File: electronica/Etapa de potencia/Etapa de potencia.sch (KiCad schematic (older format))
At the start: 20 parts

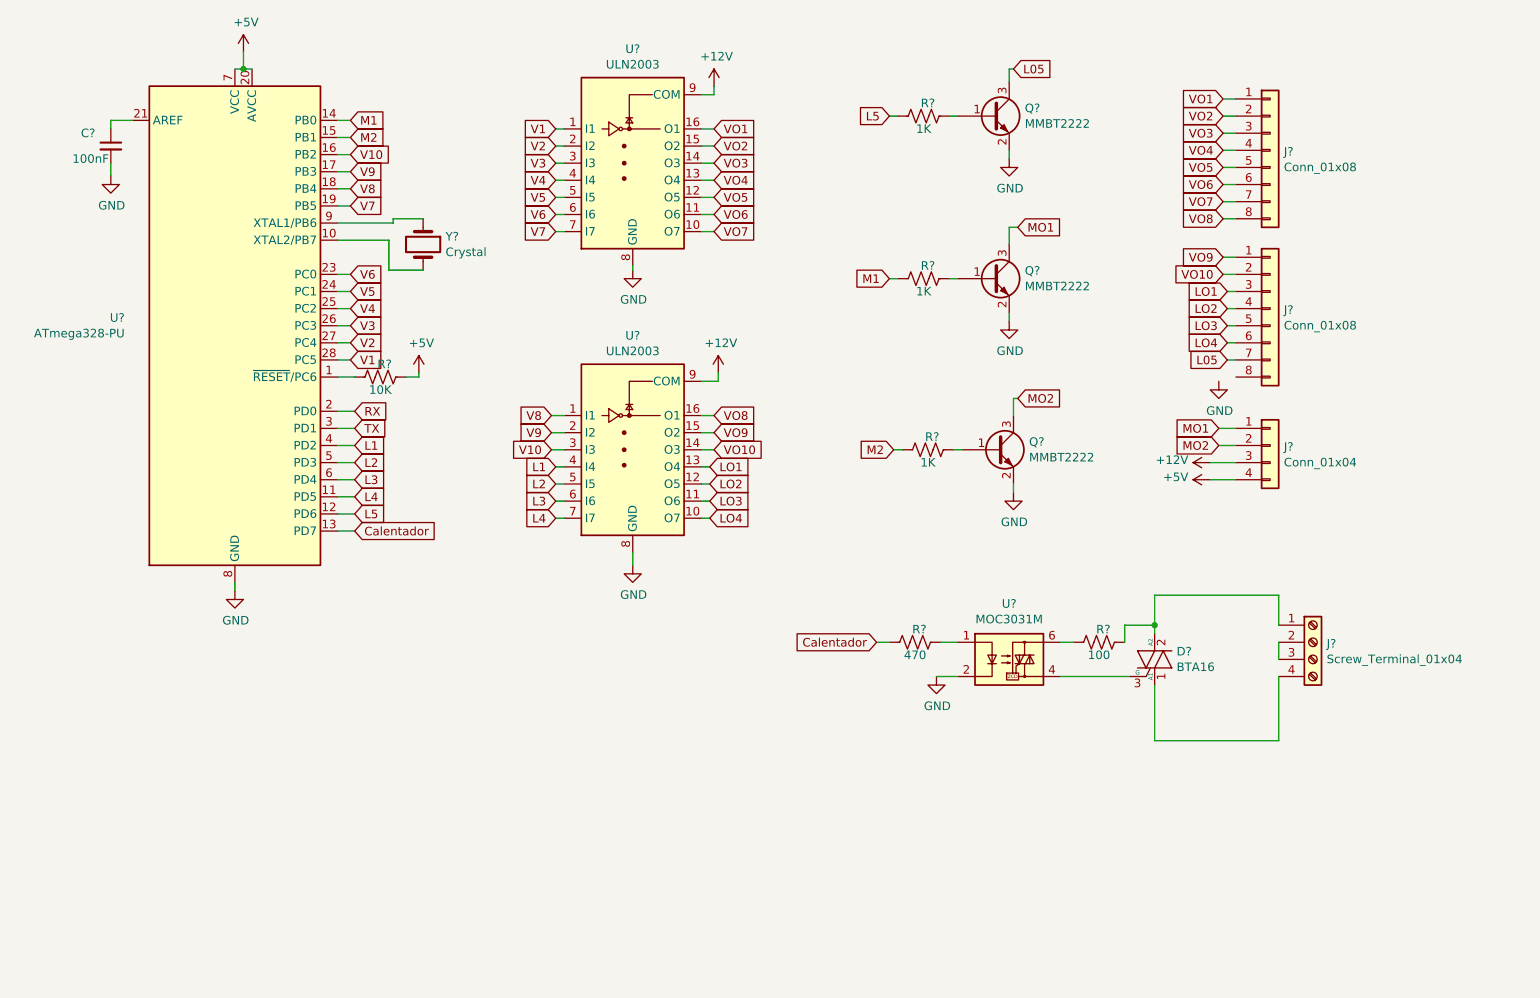
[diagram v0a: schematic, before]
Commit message: Power Stage PCB ready to revision
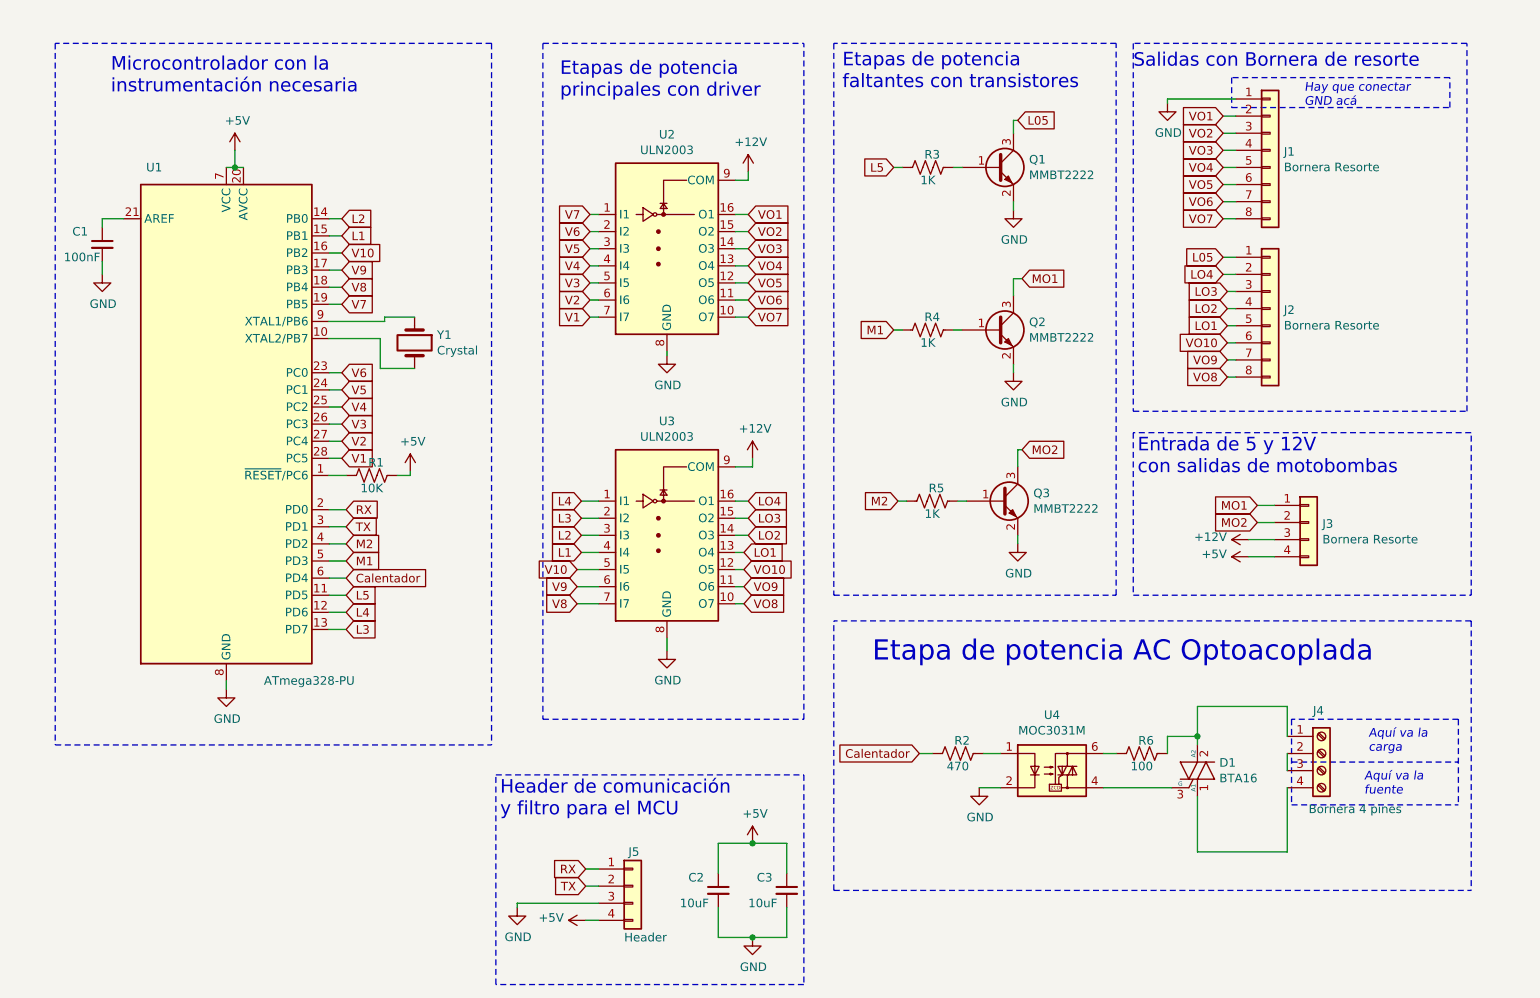
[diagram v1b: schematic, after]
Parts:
- added C2, C3: 10uF, Capacitor_SMD:C_0805_2012Metric_Pad1.15x1.40mm_HandSolder, symbol Device:C_Small
- added J5: Header, Connector_PinHeader_2.54mm:PinHeader_1x04_P2.54mm_Vertical, symbol Connector_Generic:Conn_01x04
- C1: renamed from C?; footprint (none) -> Capacitor_SMD:C_0805_2012Metric_Pad1.15x1.40mm_HandSolder
- D1: renamed from D?; footprint (none) -> Package_TO_SOT_THT:TO-220-3_Horizontal_TabDown
- J1, J2: renamed from J?; value Conn_01x08 -> Bornera Resorte; footprint (none) -> potenciaFootprints:BorneraKF141R_8Pins
- J3: renamed from J?; value Conn_01x04 -> Bornera Resorte; footprint (none) -> potenciaFootprints:BorneraKF141R_4Pins
- J4: renamed from J?; value Screw_Terminal_01x04 -> Bornera 4 pines; footprint (none) -> TerminalBlock:TerminalBlock_Altech_AK300-4_P5.00mm
- R1, R2, R3, R4, R5: renamed from R?; footprint (none) -> Resistor_SMD:R_0805_2012Metric_Pad1.15x1.40mm_HandSolder
- R6: renamed from R?; footprint (none) -> Resistor_THT:R_Axial_DIN0411_L9.9mm_D3.6mm_P12.70mm_Horizontal
- U2, U3: renamed from U?; footprint (none) -> Package_SO:SOIC-16W_5.3x10.2mm_P1.27mm
- U4: renamed from U?; footprint (none) -> Package_DIP:DIP-6_W7.62mm_LongPads
- Y1: renamed from Y?; footprint (none) -> Crystal:Crystal_SMD_0603-2Pin_6.0x3.5mm
- gave numbers to parts that had none: 4
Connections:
- net +5V: now also C2.1, C3.1, J5.4 (Pin_4)
- net Calentador: now also U1.6 (PD4); no longer U1.13 (PD7)
- net GND: now also J1.1 (Pin_1), C2.2, C3.2, J5.3 (Pin_3)
- net L05: now also J2.1 (Pin_1); no longer J2.7 (Pin_7)
- net L1: now also U1.15 (PB1); no longer U1.4 (PD2)
- net L2: now also U1.14 (PB0), U3.3 (I3); no longer U1.5 (PD3), U3.5 (I5)
- net L3: now also U1.13 (PD7), U3.2 (I2); no longer U1.6 (PD4), U3.6 (I6)
- net L4: now also U1.12 (PD6), U3.1 (I1); no longer U1.11 (PD5), U3.7 (I7)
- net L5: now also U1.11 (PD5); no longer U1.12 (PD6)
- net LO1: now also J2.5 (Pin_5); no longer J2.3 (Pin_3)
- net LO2: now also U3.14 (O3); no longer U3.12 (O5)
- net LO3: now also J2.3 (Pin_3), U3.15 (O2); no longer J2.5 (Pin_5), U3.11 (O6)
- net LO4: now also J2.2 (Pin_2), U3.16 (O1); no longer J2.6 (Pin_6), U3.10 (O7)
- net M1: now also U1.5 (PD3); no longer U1.14 (PB0)
- net M2: now also U1.4 (PD2); no longer U1.15 (PB1)
- net RX: now also J5.1 (Pin_1)
- net TX: now also J5.2 (Pin_2)
- net V1: now also U2.7 (I7); no longer U2.1 (I1)
- net V10: now also U3.5 (I5); no longer U3.3 (I3)
- net V2: now also U2.6 (I6); no longer U2.2 (I2)
- net V3: now also U2.5 (I5); no longer U2.3 (I3)
- net V5: now also U2.3 (I3); no longer U2.5 (I5)
- net V6: now also U2.2 (I2); no longer U2.6 (I6)
- net V7: now also U2.1 (I1); no longer U2.7 (I7)
- net V8: now also U3.7 (I7); no longer U3.1 (I1)
- net V9: now also U3.6 (I6); no longer U3.2 (I2)
- net VO1: now also J1.2 (Pin_2); no longer J1.1 (Pin_1)
- net VO10: now also J2.6 (Pin_6), U3.12 (O5); no longer J2.2 (Pin_2), U3.14 (O3)
- net VO2: now also J1.3 (Pin_3); no longer J1.2 (Pin_2)
- net VO3: now also J1.4 (Pin_4); no longer J1.3 (Pin_3)
- net VO4: now also J1.5 (Pin_5); no longer J1.4 (Pin_4)
- net VO5: now also J1.6 (Pin_6); no longer J1.5 (Pin_5)
- net VO6: now also J1.7 (Pin_7); no longer J1.6 (Pin_6)
- net VO7: now also J1.8 (Pin_8); no longer J1.7 (Pin_7)
- net VO8: now also J2.8 (Pin_8), U3.10 (O7); no longer J1.8 (Pin_8), U3.16 (O1)
- net VO9: now also J2.7 (Pin_7), U3.11 (O6); no longer J2.1 (Pin_1), U3.15 (O2)
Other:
- note added: "Aquí va la \ncarga"
- note added: "Aquí va la \nfuente\n"
- note added: "Entrada de 5 y 12V\ncon salidas de motobombas\n"
- note added: "Etapa de potencia AC Optoacoplada"
- note added: "Etapas de potencia \nfaltantes con transistores"
- note added: "Etapas de potencia \nprincipales con driver"
- note added: "Hay que conectar \nGND acá"
- note added: "Header de comunicación\ny filtro para el MCU"
- note added: "Microcontrolador con la\ninstrumentación necesaria"
- note added: "Salidas con Bornera de resorte"
- moved on the sheet: C1, D1, J3, J4, Q1, Q2, Q3, R1, R2, R3, R4, R5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
